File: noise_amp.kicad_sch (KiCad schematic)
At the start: 25 parts, among them J15 NOISE_EN, J16 NOISE_X121, J17 NOISE_X1331, U5 OPA4388IDR

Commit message: Remove stray power flag on N_IN and redraw its wire
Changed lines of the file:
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@@
-	)
-	(junction
-		(at 59.69 48.26)
-		(diameter 0)
-		(color 0 0 0 0)
 	)
 	(junction
@@
 	(wire
 		(pts
-			(xy 59.69 46.99) (xy 59.69 48.26)
-		)
-		(stroke
-			(width 0)
-			(type default)
-		)
-	)
-	(wire
-		(pts
 			(xy 172.72 123.19) (xy 173.99 123.19)
 		)
@@
 	(wire
 		(pts
-			(xy 53.34 39.37) (xy 53.34 48.26)
+			(xy 53.34 39.37) (xy 53.34 44.45)
 		)
 		(stroke
@@
 	(wire
 		(pts
+			(xy 53.34 44.45) (xy 69.85 44.45)
+		)
+		(stroke
+			(width 0)
+			(type default)
+		)
+	)
+	(wire
+		(pts
 			(xy 29.21 64.77) (xy 29.21 66.04)
 		)
@@
 	(wire
 		(pts
-			(xy 59.69 48.26) (xy 68.58 48.26)
-		)
-		(stroke
-			(width 0)
-			(type default)
-		)
-	)
-	(wire
-		(pts
 			(xy 162.56 123.19) (xy 165.1 123.19)
 		)
@@
 	(wire
 		(pts
-			(xy 53.34 48.26) (xy 59.69 48.26)
-		)
-		(stroke
-			(width 0)
-			(type default)
-		)
-	)
-	(wire
-		(pts
 			(xy 128.27 81.28) (xy 133.35 81.28)
 		)
@@
 	)
 	(label "N_IN"
-		(at 64.77 48.26 0)
+		(at 64.77 44.45 0)
 		(effects
 			(font
@@
 			)
 		)
-	)
-	(symbol
-		(lib_id "power:PWR_FLAG")
-		(at 59.69 46.99 0)
-		(unit 1)
-		(body_style 1)
-		(exclude_from_sim no)
-		(in_bom yes)
-		(on_board yes)
-		(in_pos_files yes)
-		(dnp no)
-		(fields_autoplaced yes)
-		(property "Reference" "#FLG07"
-			(at 59.69 45.085 0)
-			(hide yes)
-			(show_name no)
-			(do_not_autoplace no)
-			(effects
-				(font
-					(size 1.27 1.27)
-				)
-			)
-		)
-		(property "Value" "PWR_FLAG"
-			(at 59.69 41.91 0)
-			(show_name no)
-			(do_not_autoplace no)
-			(effects
-				(font
-					(size 1.27 1.27)
-				)
-			)
-		)
-		(property "Footprint" ""
-			(at 59.69 46.99 0)
-			(hide yes)
-			(show_name no)
-			(do_not_autoplace no)
-			(effects
-				(font
-					(size 1.27 1.27)
-				)
-			)
-		)
-		(property "Datasheet" ""
-			(at 59.69 46.99 0)
-			(hide yes)
-			(show_name no)
-			(do_not_autoplace no)
-			(effects
-				(font
-					(size 1.27 1.27)
-				)
-			)
-		)
-		(property "Description" "Special symbol for telling ERC where power comes from"
-			(at 59.69 46.99 0)
-			(hide yes)
-			(show_name no)
-			(do_not_autoplace no)
-			(effects
-				(font
-					(size 1.27 1.27)
-				)
-			)
-		)
-		(pin "1"
-		)
-		(instances
-			(project "ldo_bringup_board_ee372"
-				(path "/d41ff68c-d87d-4b82-b500-4ee675d17cf6/865f8bee-21ea-4e12-aa41-2d2ad2cc6c72"
-					(reference "#FLG07")
-					(unit 1)
-				)
-			)
-		)

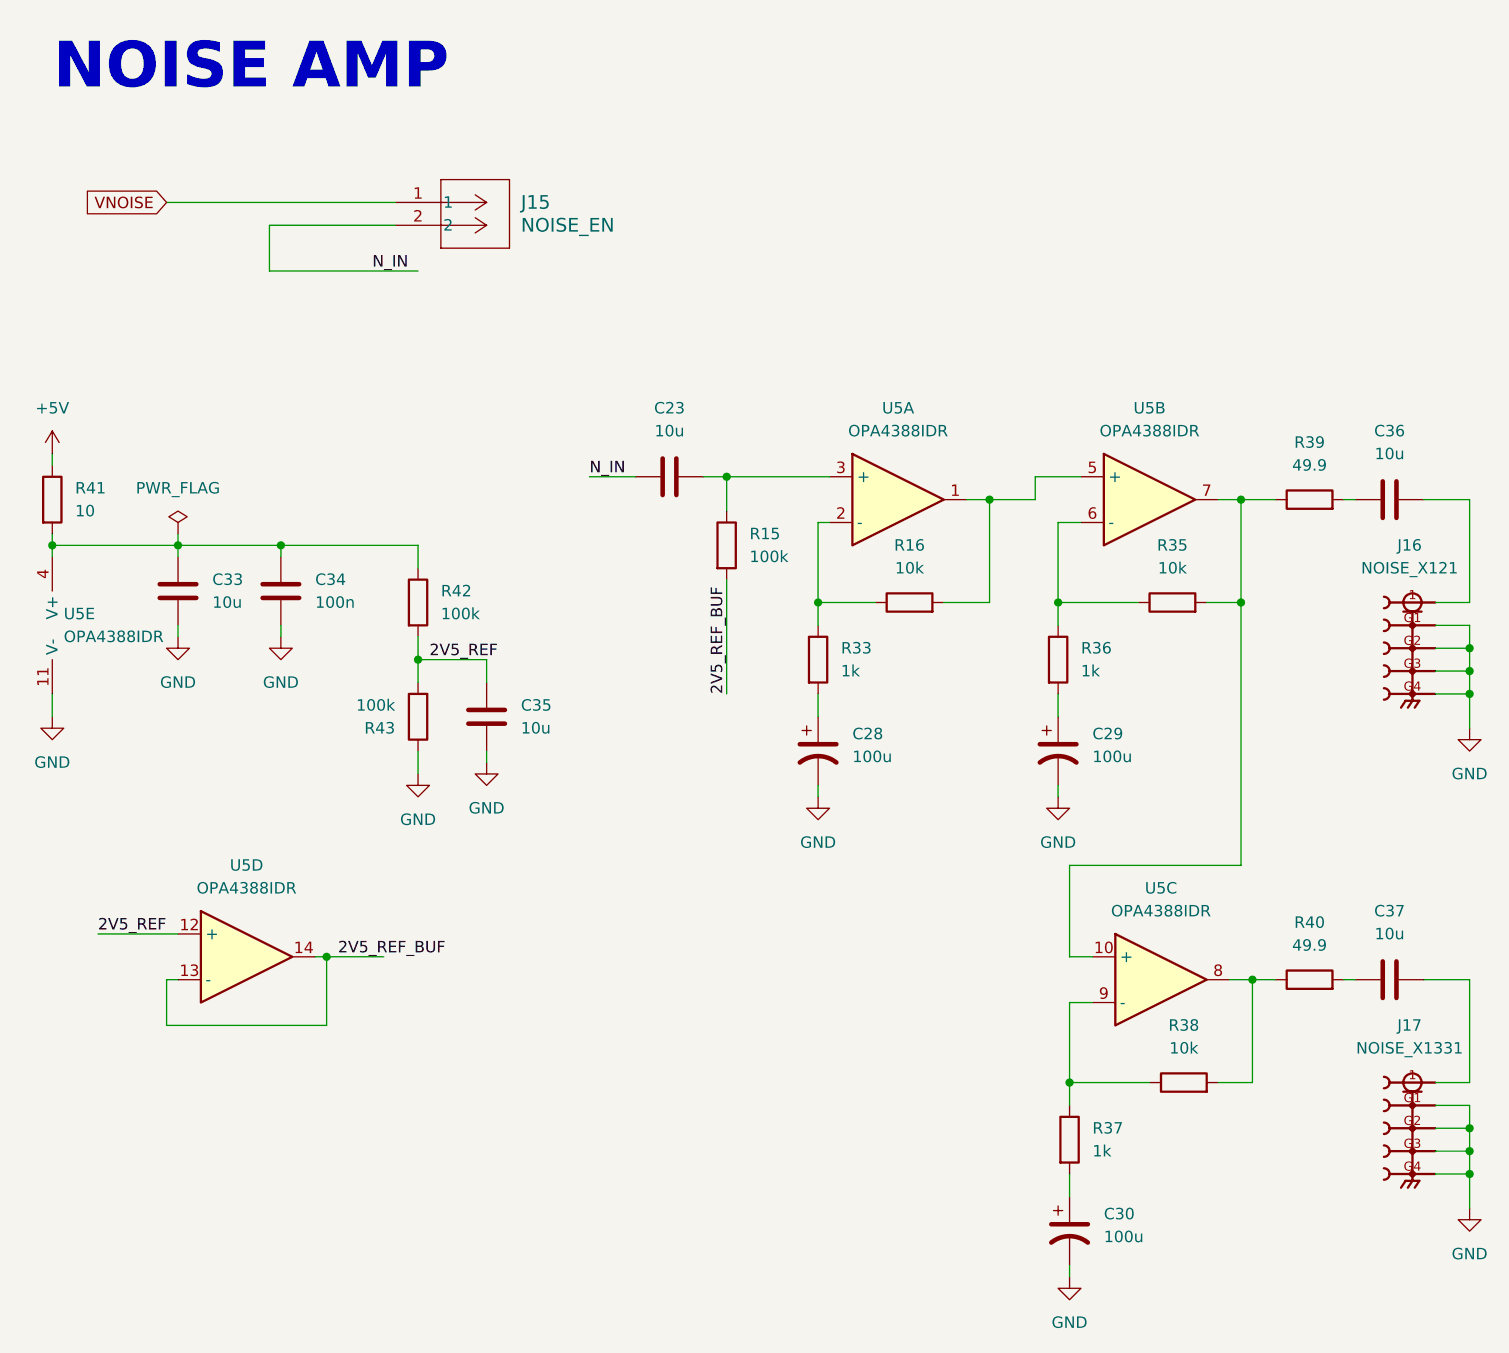
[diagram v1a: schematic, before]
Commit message: Replace J15 noise enable header with 0 ohm R44
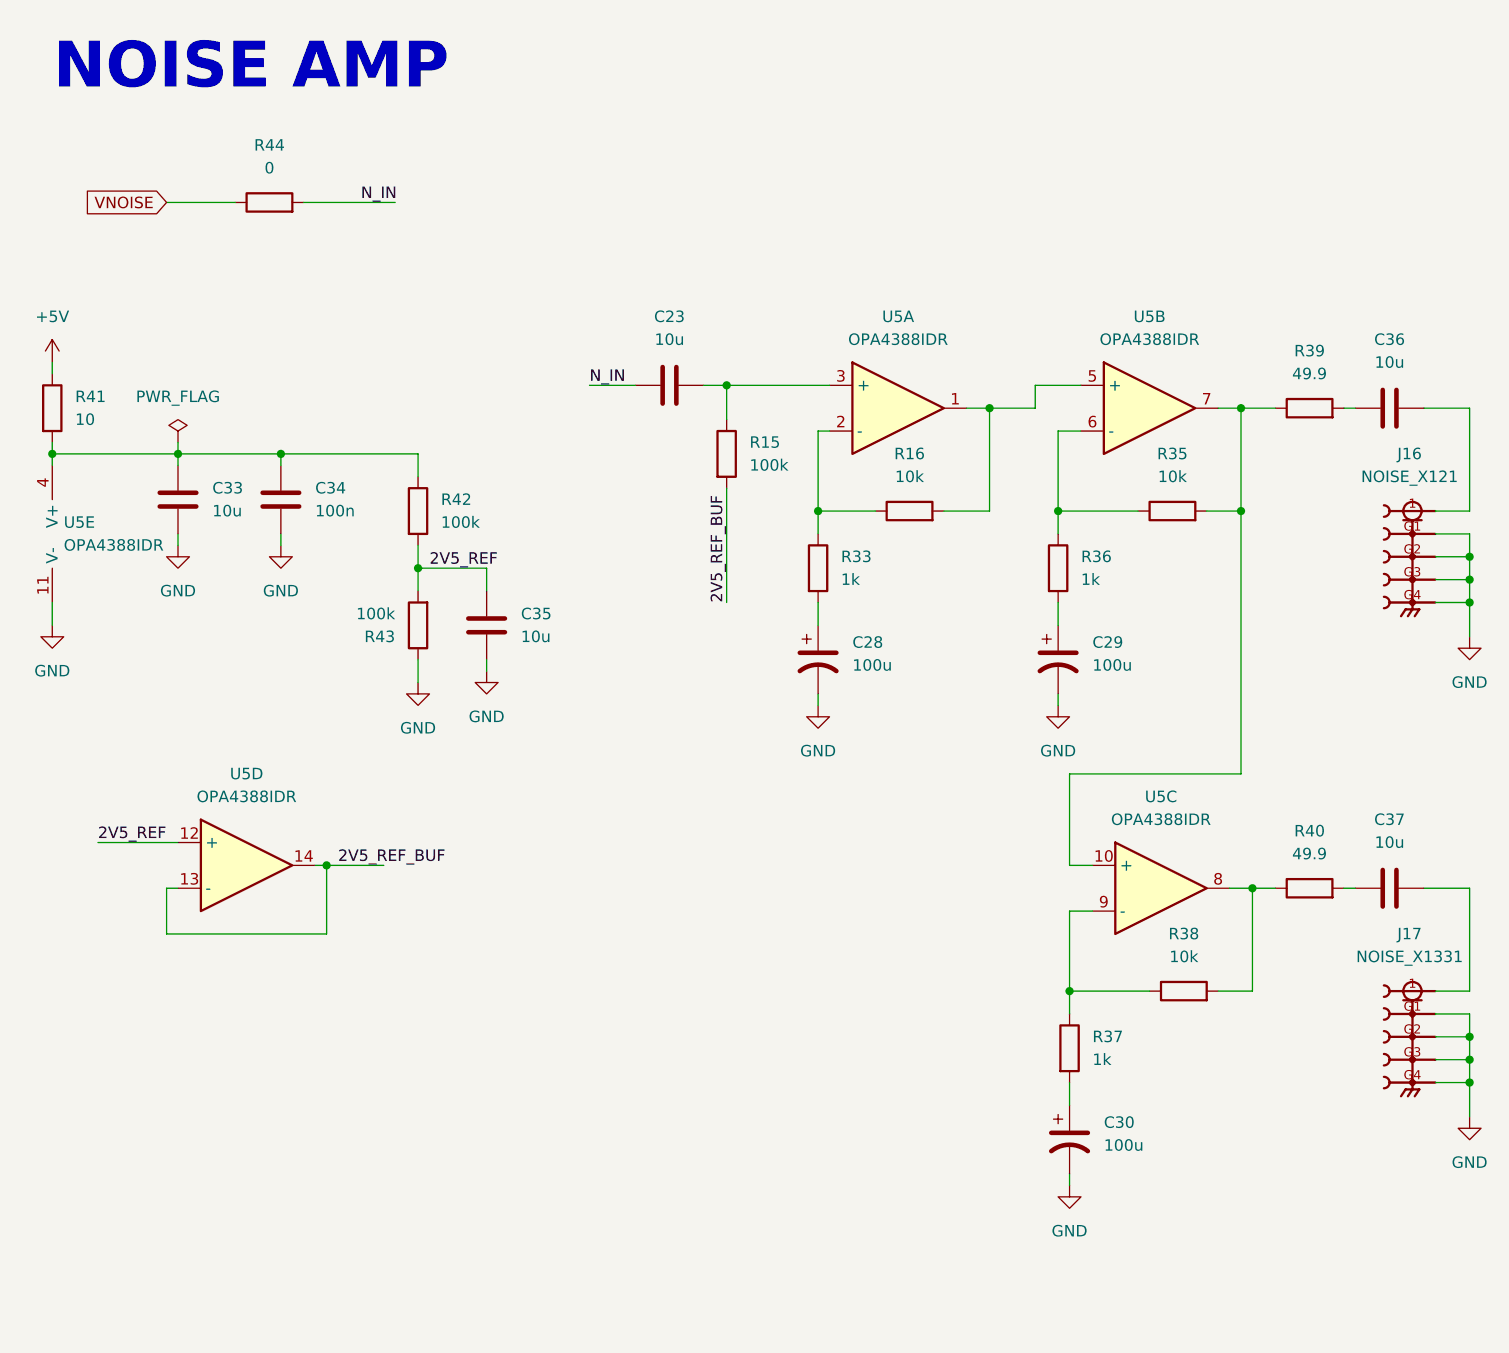
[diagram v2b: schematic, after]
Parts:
- removed J15: NOISE_EN, ldo_bringup_board_ee372:CONN_PxC02S_SUL, symbol ldo_bringup_board_ee372:PEC02SAAN
- added R44: 0, Resistor_SMD:R_0805_2012Metric_Pad1.20x1.40mm_HandSolder, symbol Device:R
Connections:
- net N_IN: now also R44.2
- net VNOISE: now also R44.1
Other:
- moved on the sheet: C23, C28, C29, C30, C33, C34, C35, C36, C37, J16, J17, R15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

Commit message: Change noise amp feedback to 9k and outputs to 0 ohm, add NR jack and test point
Noise amplifier sheet:
- R16, R35, R38 changed from 10k to 9k
- R39, R40 (49.9 ohm) removed; R49, R50 (0 ohm) placed between the U5
  stage outputs and C36, C37
- J16, J17 values renamed NOISE_X100 and NOISE_X1000

Top sheet:
- TP30 added on NR
- J15 banana jack added, joined to NR through R39 (0 ohm, DNP)
- SW1 value renamed MD_SW
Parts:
- removed R39, R40: 49.9, Resistor_SMD:R_0805_2012Metric_Pad1.20x1.40mm_HandSolder, symbol Device:R
- added R49, R50: 0, Resistor_SMD:R_0805_2012Metric_Pad1.20x1.40mm_HandSolder, symbol Device:R
- J16: value NOISE_X121 -> NOISE_X100
- J17: value NOISE_X1331 -> NOISE_X1000
- R16, R35, R38: value 10k -> 9k
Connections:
- net at R35.2, U5.10 (+), U5.7: now also R49.1
- net at R38.2, U5.8: now also R50.1
- net at C36.1: now also R49.2
- net at C37.1: now also R50.2
